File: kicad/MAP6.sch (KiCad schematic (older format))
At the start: 26 parts, among them M1 Motor_vibration, P1 Logo_MA, P2 Pin, P3 LEG, P4 LEG, P5 LEG, P6 LEG, P7 LEG, P8 LEG, P9 STING, Q1 BC547, SW1 On, U1 LM555

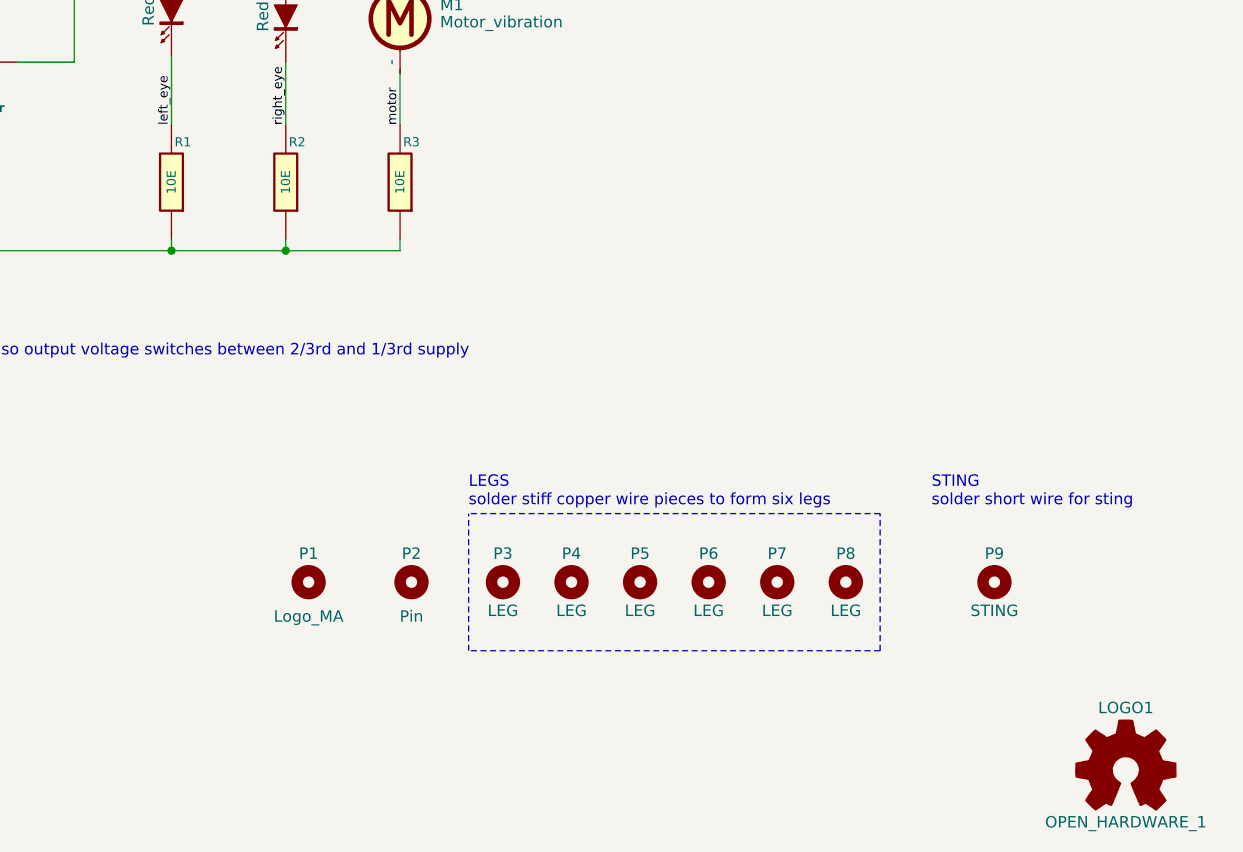
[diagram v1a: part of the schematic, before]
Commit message: added interactive HTML BoM in /bom folder
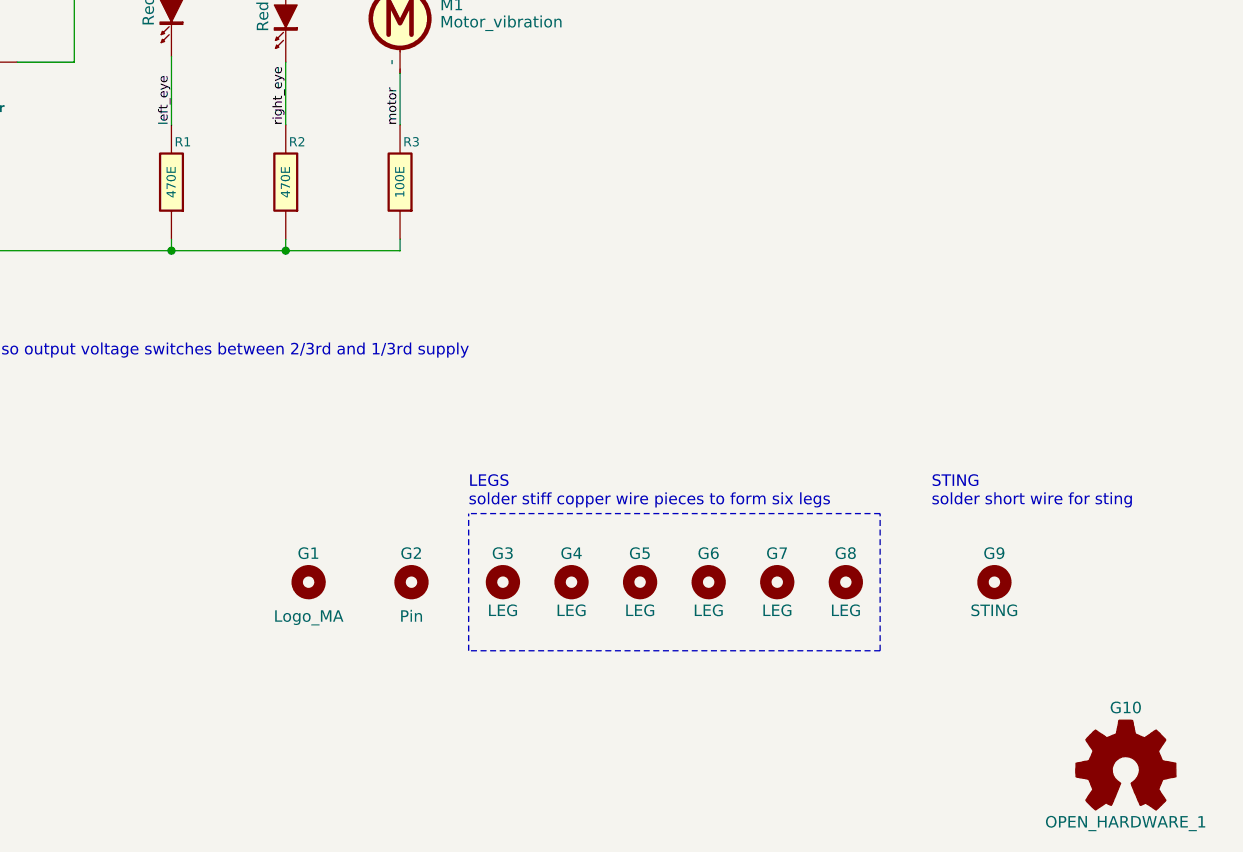
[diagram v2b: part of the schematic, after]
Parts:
- R1, R2: value 10E -> 470E
- R3: value 10E -> 100E
- renumbered P1 to G1, LOGO1 to G10, P2 to G2, P3 to G3, P4 to G4, P5 to G5, P6 to G6, P7 to G7, P8 to G8, P9 to G9
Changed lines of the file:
@@
 P 6600 4300
 F 0 "R1" H 6550 4125 40  0000 C CNN
-F 1 "10E" V 6600 4300 40  0000 C CNN
+F 1 "470E" V 6600 4300 40  0000 C CNN
 F 2 "map6_fp:r_0805" V 6530 4300 50  0001 C CNN
 F 3 "" H 6600 4300 50  0000 C CNN
@@
 P 7100 4300
 F 0 "R2" H 7050 4125 40  0000 C CNN
-F 1 "10E" V 7100 4300 40  0000 C CNN
+F 1 "470E" V 7100 4300 40  0000 C CNN
 F 2 "map6_fp:r_0805" V 7030 4300 50  0001 C CNN
 F 3 "" H 7100 4300 50  0000 C CNN
@@
 P 7600 4300
 F 0 "R3" H 7550 4125 40  0000 C CNN
-F 1 "10E" V 7600 4300 40  0000 C CNN
+F 1 "100E" V 7600 4300 40  0000 C CNN
 F 2 "map6_fp:r_0805" V 7530 4300 50  0001 C CNN
 F 3 "" H 7600 4300 50  0000 C CNN
@@
 	6600 4550 6600 4600
 $Comp
-L map6:OPEN_HARDWARE_1 LOGO1
+L map6:OPEN_HARDWARE_1 G10
 U 1 1 57444ACD
 P 10775 6875
-F 0 "LOGO1" H 10775 7150 50  0000 C CNN
+F 0 "G10" H 10775 7150 50  0000 C CNN
 F 1 "OPEN_HARDWARE_1" H 10775 6650 50  0000 C CNN
 F 2 "map6_fp:Logo_silk_OSHW_6x6mm" H 10775 6875 60  0001 C CNN
@@
 $EndComp
 $Comp
-L map6:MountingHole P1
+L map6:MountingHole G1
 U 1 1 57444C89
 P 7200 6050
-F 0 "P1" V 7075 6050 50  0000 C CNN
+F 0 "G1" V 7075 6050 50  0000 C CNN
 F 1 "Logo_MA" V 7350 6050 50  0000 C CNN
 F 2 "map6_fp:MA_LOGO" H 7200 6050 50  0001 C CNN
@@
 $EndComp
 $Comp
-L map6:MountingHole P2
+L map6:MountingHole G2
 U 1 1 57444D7F
 P 7650 6050
-F 0 "P2" V 7525 6050 50  0000 C CNN
+F 0 "G2" V 7525 6050 50  0000 C CNN
 F 1 "Pin" V 7800 6050 50  0000 C CNN
 F 2 "map6_fp:MTG_2mm" H 7650 6050 50  0001 C CNN
@@
 motor
 $Comp
-L map6:MountingHole P3
+L map6:MountingHole G3
 U 1 1 574578C5
 P 8050 6050
-F 0 "P3" V 7925 6050 50  0000 C CNN
+F 0 "G3" V 7925 6050 50  0000 C CNN
 F 1 "LEG" V 8175 6050 50  0000 C CNN
 F 2 "map6_fp:MTG_1mm" H 8050 6050 50  0001 C CNN
@@
 $EndComp
 $Comp
-L map6:MountingHole P4
+L map6:MountingHole G4
 U 1 1 574578FE
 P 8350 6050
-F 0 "P4" V 8225 6050 50  0000 C CNN
+F 0 "G4" V 8225 6050 50  0000 C CNN
 F 1 "LEG" V 8475 6050 50  0000 C CNN
 F 2 "map6_fp:MTG_1mm" H 8350 6050 50  0001 C CNN
@@
 $EndComp
 $Comp
-L map6:MountingHole P5
+L map6:MountingHole G5
 U 1 1 57457995
 P 8650 6050
-F 0 "P5" V 8525 6050 50  0000 C CNN
+F 0 "G5" V 8525 6050 50  0000 C CNN
 F 1 "LEG" V 8775 6050 50  0000 C CNN
 F 2 "map6_fp:MTG_1mm" H 8650 6050 50  0001 C CNN
@@
 $EndComp
 $Comp
-L map6:MountingHole P6
+L map6:MountingHole G6
 U 1 1 5745799C
 P 8950 6050
-F 0 "P6" V 8825 6050 50  0000 C CNN
+F 0 "G6" V 8825 6050 50  0000 C CNN
 F 1 "LEG" V 9075 6050 50  0000 C CNN
 F 2 "map6_fp:MTG_1mm" H 8950 6050 50  0001 C CNN
@@
 $EndComp
 $Comp
-L map6:MountingHole P7
+L map6:MountingHole G7
 U 1 1 611BDF21
 P 9250 6050
-F 0 "P7" V 9125 6050 50  0000 C CNN
+F 0 "G7" V 9125 6050 50  0000 C CNN
 F 1 "LEG" V 9375 6050 50  0000 C CNN
 F 2 "map6_fp:MTG_1mm" H 9250 6050 50  0001 C CNN
@@
 $EndComp
 $Comp
-L map6:MountingHole P8
+L map6:MountingHole G8
 U 1 1 611BDFB5
 P 9550 6050
-F 0 "P8" V 9425 6050 50  0000 C CNN
+F 0 "G8" V 9425 6050 50  0000 C CNN
 F 1 "LEG" V 9675 6050 50  0000 C CNN
 F 2 "map6_fp:MTG_1mm" H 9550 6050 50  0001 C CNN
@@
 $EndComp
 $Comp
-L map6:MountingHole P9
+L map6:MountingHole G9
 U 1 1 61224D24
 P 10200 6050
-F 0 "P9" V 10075 6050 50  0000 C CNN
+F 0 "G9" V 10075 6050 50  0000 C CNN
 F 1 "STING" V 10325 6050 50  0000 C CNN
 F 2 "map6_fp:MTG_0mm8" H 10200 6050 50  0001 C CNN

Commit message: updated schematic and pcb
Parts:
- G1: symbol map6:MountingHole -> map6:H_Logo_MA_2
- G2: symbol map6:MountingHole -> map6:H_Pin
- G3, G4, G5, G6, G7, G8: symbol map6:MountingHole -> map6:H_brd
- R1, R2: value 470E -> 150E
- R3: value 100E -> 15E
- R4, R6: footprint map6_fp:r_0805 -> map6_fp:r_0805_DNP
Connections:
- net at D1.1 (A), D2.1 (A), Q1.3 (E): no longer M1.1 (+)
- net at JP1.2 (B), Q1.2 (B), R5.1: now also M1.1 (+)
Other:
- moved on the sheet: D1, D2, M1, R1, R2, R3
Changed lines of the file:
@@
 L map6:LED D1
 U 1 1 570F5ABC
-P 6600 3550
-F 0 "D1" V 6500 3625 50  0000 C CNN
-F 1 "Red" H 6600 3450 50  0000 C CNN
-F 2 "map6_fp:LED-5MM_left" H 6600 3550 50  0001 C CNN
-F 3 "" H 6600 3550 50  0000 C CNN
-	1    6600 3550
+P 7100 3575
+F 0 "D1" V 7000 3650 50  0000 C CNN
+F 1 "Red" H 7100 3475 50  0000 C CNN
+F 2 "map6_fp:LED-5MM_left" H 7100 3575 50  0001 C CNN
+F 3 "" H 7100 3575 50  0000 C CNN
+	1    7100 3575
 	0    1    1    0
 $EndComp
@@
 L map6:LED D2
 U 1 1 570F5B5A
-P 7100 3575
-F 0 "D2" V 7000 3650 50  0000 C CNN
-F 1 "Red" H 7100 3475 50  0000 C CNN
-F 2 "map6_fp:LED-5MM_right" H 7100 3575 50  0001 C CNN
-F 3 "" H 7100 3575 50  0000 C CNN
-	1    7100 3575
+P 7600 3575
+F 0 "D2" V 7500 3650 50  0000 C CNN
+F 1 "Red" H 7600 3475 50  0000 C CNN
+F 2 "map6_fp:LED-5MM_right" H 7600 3575 50  0001 C CNN
+F 3 "" H 7600 3575 50  0000 C CNN
+	1    7600 3575
 	0    1    1    0
 $EndComp
@@
 L map6:R R1
 U 1 1 57443D6C
+P 7100 4300
+F 0 "R1" H 7050 4125 40  0000 C CNN
+F 1 "150E" V 7100 4300 40  0000 C CNN
+F 2 "map6_fp:r_0805" V 7030 4300 50  0001 C CNN
+F 3 "" H 7100 4300 50  0000 C CNN
+F 4 "Value" H 7100 4300 60  0001 C CNN "manf#"
+	1    7100 4300
+	-1   0    0    1
+$EndComp
+$Comp
+L map6:R R2
+U 1 1 57443E35
+P 7600 4300
+F 0 "R2" H 7550 4125 40  0000 C CNN
+F 1 "150E" V 7600 4300 40  0000 C CNN
+F 2 "map6_fp:r_0805" V 7530 4300 50  0001 C CNN
+F 3 "" H 7600 4300 50  0000 C CNN
+F 4 "Value" H 7600 4300 60  0001 C CNN "manf#"
+	1    7600 4300
+	-1   0    0    1
+$EndComp
+$Comp
+L map6:R R3
+U 1 1 57443E83
 P 6600 4300
-F 0 "R1" H 6550 4125 40  0000 C CNN
-F 1 "470E" V 6600 4300 40  0000 C CNN
+F 0 "R3" H 6550 4125 40  0000 C CNN
+F 1 "15E" V 6600 4300 40  0000 C CNN
 F 2 "map6_fp:r_0805" V 6530 4300 50  0001 C CNN
 F 3 "" H 6600 4300 50  0000 C CNN
@@
 	-1   0    0    1
 $EndComp
-$Comp
-L map6:R R2
-U 1 1 57443E35
-P 7100 4300
-F 0 "R2" H 7050 4125 40  0000 C CNN
-F 1 "470E" V 7100 4300 40  0000 C CNN
-F 2 "map6_fp:r_0805" V 7030 4300 50  0001 C CNN
-F 3 "" H 7100 4300 50  0000 C CNN
-F 4 "Value" H 7100 4300 60  0001 C CNN "manf#"
-	1    7100 4300
-	-1   0    0    1
-$EndComp
-$Comp
-L map6:R R3
-U 1 1 57443E83
-P 7600 4300
-F 0 "R3" H 7550 4125 40  0000 C CNN
-F 1 "100E" V 7600 4300 40  0000 C CNN
-F 2 "map6_fp:r_0805" V 7530 4300 50  0001 C CNN
-F 3 "" H 7600 4300 50  0000 C CNN
-F 4 "Value" H 7600 4300 60  0001 C CNN "manf#"
-	1    7600 4300
-	-1   0    0    1
-$EndComp
 Wire Wire Line
 	2725 1025 4025 1025
 Wire Wire Line
-	6600 3275 6600 3350
-Wire Wire Line
-	7600 3275 7600 3325
+	7600 3275 7600 3375
 Wire Wire Line
 	7100 3375 7100 3275
 Connection ~ 7100 3275
 Wire Wire Line
-	6600 3750 6600 4050
-Wire Wire Line
 	7100 3775 7100 4050
 Wire Wire Line
-	7600 3825 7600 4050
+	7600 3775 7600 4050
+Wire Wire Line
+	6600 3900 6600 4050
 Wire Wire Line
 	2725 4600 4025 4600
@@
 $EndComp
 $Comp
-L map6:MountingHole G1
+L map6:H_Logo_MA_2 G1
 U 1 1 57444C89
-P 7200 6050
-F 0 "G1" V 7075 6050 50  0000 C CNN
-F 1 "Logo_MA" V 7350 6050 50  0000 C CNN
-F 2 "map6_fp:MA_LOGO" H 7200 6050 50  0001 C CNN
-F 3 "" H 7200 6050 50  0000 C CNN
-	1    7200 6050
-	0    1    1    0
-$EndComp
-$Comp
-L map6:MountingHole G2
+P 6550 6900
+F 0 "G1" H 6550 6550 50  0000 C CNN
+F 1 "Logo_MA" H 6550 6450 50  0000 C CNN
+F 2 "map6_fp:MA_LOGO" H 6550 6900 50  0001 C CNN
+F 3 "" H 6550 6900 50  0000 C CNN
+	1    6550 6900
+	1    0    0    -1
+$EndComp
+$Comp
+L map6:H_Pin G2
 U 1 1 57444D7F
-P 7650 6050
-F 0 "G2" V 7525 6050 50  0000 C CNN
-F 1 "Pin" V 7800 6050 50  0000 C CNN
-F 2 "map6_fp:MTG_2mm" H 7650 6050 50  0001 C CNN
-F 3 "" H 7650 6050 50  0000 C CNN
-	1    7650 6050
-	0    1    1    0
+P 6475 6050
+F 0 "G2" H 6475 5925 50  0000 C CNN
+F 1 "Pin" H 6475 5825 50  0000 C CNN
+F 2 "map6_fp:MTG_2mm" H 6475 6050 50  0001 C CNN
+F 3 "" H 6475 6050 50  0000 C CNN
+	1    6475 6050
+	1    0    0    -1
 $EndComp
 Text Label 3425 1025 0    50   ~ 10
@@
 Text Label 3425 4600 0    50   ~ 10
 GND
+Text Label 7100 4050 1    40   ~ 0
+left_eye
+Text Label 7600 4050 1    40   ~ 0
+right_eye
 Text Label 6600 4050 1    40   ~ 0
-left_eye
-Text Label 7100 4050 1    40   ~ 0
-right_eye
-Text Label 7600 4050 1    40   ~ 0
 motor
 $Comp
-L map6:MountingHole G3
+L map6:H_brd G3
 U 1 1 574578C5
-P 8050 6050
-F 0 "G3" V 7925 6050 50  0000 C CNN
-F 1 "LEG" V 8175 6050 50  0000 C CNN
-F 2 "map6_fp:MTG_1mm" H 8050 6050 50  0001 C CNN
-F 3 "" H 8050 6050 50  0000 C CNN
-	1    8050 6050
-	0    1    1    0
-$EndComp
-$Comp
-L map6:MountingHole G4
+P 7000 5875
+F 0 "G3" H 7000 5575 50  0000 C CNN
+F 1 "LEG" H 7000 5500 50  0000 C CNN
+F 2 "map6_fp:MTG_1mm" H 7000 5875 50  0001 C CNN
+F 3 "" H 7000 5875 50  0000 C CNN
+	1    7000 5875
+	1    0    0    -1
+$EndComp
+$Comp
+L map6:H_brd G4
 U 1 1 574578FE
-P 8350 6050
-F 0 "G4" V 8225 6050 50  0000 C CNN
-F 1 "LEG" V 8475 6050 50  0000 C CNN
-F 2 "map6_fp:MTG_1mm" H 8350 6050 50  0001 C CNN
-F 3 "" H 8350 6050 50  0000 C CNN
-	1    8350 6050
-	0    1    1    0
-$EndComp
-$Comp
-L map6:MountingHole G5
+P 7525 5875
+F 0 "G4" H 7525 5575 50  0000 C CNN
+F 1 "LEG" H 7525 5500 50  0000 C CNN
+F 2 "map6_fp:MTG_1mm" H 7525 5875 50  0001 C CNN
+F 3 "" H 7525 5875 50  0000 C CNN
+	1    7525 5875
+	1    0    0    -1
+$EndComp
+$Comp
+L map6:H_brd G5
 U 1 1 57457995
-P 8650 6050
-F 0 "G5" V 8525 6050 50  0000 C CNN
-F 1 "LEG" V 8775 6050 50  0000 C CNN
-F 2 "map6_fp:MTG_1mm" H 8650 6050 50  0001 C CNN
-F 3 "" H 8650 6050 50  0000 C CNN
-	1    8650 6050
-	0    1    1    0
-$EndComp
-$Comp
-L map6:MountingHole G6
+P 8050 5875
+F 0 "G5" H 8050 5575 50  0000 C CNN
+F 1 "LEG" H 8050 5500 50  0000 C CNN
+F 2 "map6_fp:MTG_1mm" H 8050 5875 50  0001 C CNN
+F 3 "" H 8050 5875 50  0000 C CNN
+	1    8050 5875
+	1    0    0    -1
+$EndComp
+$Comp
+L map6:H_brd G6
 U 1 1 5745799C
-P 8950 6050
-F 0 "G6" V 8825 6050 50  0000 C CNN
-F 1 "LEG" V 9075 6050 50  0000 C CNN
-F 2 "map6_fp:MTG_1mm" H 8950 6050 50  0001 C CNN
-F 3 "" H 8950 6050 50  0000 C CNN
-	1    8950 6050
-	0    1    1    0
-$EndComp
-Wire Wire Line
-	6600 3275 7100 3275
+P 8575 5875
+F 0 "G6" H 8575 5575 50  0000 C CNN
+F 1 "LEG" H 8575 5500 50  0000 C CNN
+F 2 "map6_fp:MTG_1mm" H 8575 5875 50  0001 C CNN
+F 3 "" H 8575 5875 50  0000 C CNN
+	1    8575 5875
+	1    0    0    -1
+$EndComp
 Wire Wire Line
 	7100 3275 7600 3275
@@
 L map6:Motor_DC M1
 U 1 1 6118D8BD
-P 7600 3525
-F 0 "M1" H 7775 3525 50  0000 L CNN
-F 1 "Motor_vibration" H 7775 3450 50  0000 L CNN
-F 2 "map6_fp:motor_XDCR_C0720B001F" H 7600 3435 50  0001 C CNN
-F 3 "~" H 7600 3435 50  0001 C CNN
-	1    7600 3525
-	1    0    0    -1
-$EndComp
-$Comp
-L map6:MountingHole G7
+P 6600 3600
+F 0 "M1" H 6625 3725 50  0000 L CNN
+F 1 "Motor_vibration" V 6500 3725 50  0000 L CNN
+F 2 "map6_fp:motor_XDCR_C0720B001F" H 6600 3510 50  0001 C CNN
+F 3 "~" H 6600 3510 50  0001 C CNN
+	1    6600 3600
+	1    0    0    -1
+$EndComp
+$Comp
+L map6:H_brd G7
 U 1 1 611BDF21
-P 9250 6050
-F 0 "G7" V 9125 6050 50  0000 C CNN
-F 1 "LEG" V 9375 6050 50  0000 C CNN
-F 2 "map6_fp:MTG_1mm" H 9250 6050 50  0001 C CNN
-F 3 "" H 9250 6050 50  0000 C CNN
-	1    9250 6050
-	0    1    1    0
-$EndComp
-$Comp
-L map6:MountingHole G8
+P 9100 5875
+F 0 "G7" H 9100 5575 50  0000 C CNN
+F 1 "LEG" H 9100 5500 50  0000 C CNN
+F 2 "map6_fp:MTG_1mm" H 9100 5875 50  0001 C CNN
+F 3 "" H 9100 5875 50  0000 C CNN
+	1    9100 5875
+	1    0    0    -1
+$EndComp
+$Comp
+L map6:H_brd G8
 U 1 1 611BDFB5
-P 9550 6050
-F 0 "G8" V 9425 6050 50  0000 C CNN
-F 1 "LEG" V 9675 6050 50  0000 C CNN
-F 2 "map6_fp:MTG_1mm" H 9550 6050 50  0001 C CNN
-F 3 "" H 9550 6050 50  0000 C CNN
-	1    9550 6050
-	0    1    1    0
+P 9625 5875
+F 0 "G8" H 9625 5575 50  0000 C CNN
+F 1 "LEG" H 9625 5500 50  0000 C CNN
+F 2 "map6_fp:MTG_1mm" H 9625 5875 50  0001 C CNN
+F 3 "" H 9625 5875 50  0000 C CNN
+	1    9625 5875
+	1    0    0    -1
 $EndComp
 $Comp
@@
 F 0 "R6" H 3975 2025 40  0000 C CNB
 F 1 "DNP" V 4025 2200 40  0000 C CNB
-F 2 "map6_fp:r_0805" V 3955 2200 50  0001 C CNN
+F 2 "map6_fp:r_0805_DNP" V 3955 2200 50  0001 C CNN
 F 3 "" H 4025 2200 50  0000 C CNN
 F 4 "Value" H 4025 2200 60  0001 C CNN "manf#"
@@
 F 0 "R4" H 3975 1250 40  0000 C CNB
 F 1 "DNP" V 4025 1425 40  0000 C CNB
-F 2 "map6_fp:r_0805" V 3955 1425 50  0001 C CNN
+F 2 "map6_fp:r_0805_DNP" V 3955 1425 50  0001 C CNN
 F 3 "" H 4025 1425 50  0000 C CNN
 F 4 "Value" H 4025 1425 60  0001 C CNN "manf#"
@@
 Connection ~ 6175 2825
 Wire Wire Line
-	6175 2825 6800 2825
+	6175 2825 6600 2825
 Wire Wire Line
 	7100 3025 7100 3275
@@
 Battery Holder\n2x2032 or 2x2016\nwith switch
 Wire Notes Line width 10 rgb(255, 128, 0)
-	7900 6350 7900 5750
-Wire Notes Line width 10 rgb(255, 128, 0)
-	9700 5750 7900 5750
-Wire Notes Line width 10 rgb(255, 128, 0)
-	9700 6350 9700 5750
-Wire Notes Line width 10 rgb(255, 128, 0)
-	9700 6350 7900 6350
-Text Notes 7900 5725 0    50   ~ 0
+	6700 6350 6700 5500
+Wire Notes Line width 10 rgb(255, 128, 0)
+	9950 5500 6700 5500
+Wire Notes Line width 10 rgb(255, 128, 0)
+	9950 6350 9950 5500
+Wire Notes Line width 10 rgb(255, 128, 0)
+	9950 6350 6700 6350
+Text Notes 6700 5475 0    50   ~ 0
 LEGS\nsolder stiff copper wire pieces to form six legs
 Wire Wire Line
@@
 	0    1    1    0
 $EndComp
-Text Notes 9925 5725 0    50   ~ 0
+Text Notes 10100 5725 0    50   ~ 0
 STING\nsolder short wire for sting
+Wire Wire Line
+	6600 3400 6600 2825
+Connection ~ 6600 2825
+Wire Wire Line
+	6600 2825 6800 2825
 $EndSCHEMATC
